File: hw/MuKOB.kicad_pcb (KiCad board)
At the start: 2 copper layers, 123.2 x 125.7 mm, 121 parts, among them J1 UART0 IO01, J10 IO_EX, J11 SPKR_L, J12 SPKR_R, J13 UI 20-RBN, J14 AUDIO, J15 SPI-0, J16 SPI-DISP, J17 SW_MATRIX, J18 UIM 20-FCC, J19 UIM 20-RBN, J2 SERIAL-COMM, J3 KEY_SND_IF, J4 GPIO28, J5 I2C-0, J6 MicroSD-Socket w/Det, J7 KEY-PADDLE, J8 UART1 IO89, J9 UI 20-FCC, Q1 2N3904, SW1 RESET, SW2 RE-SO, SW3 UP, SW4 LF, SW5 EN, SW6 RT, SW7 DN, SW8 RE-AO, SW9 RE-BO, U1 MAX3221, U2 PicoW, U3 MCP23S08-E/SO, U4 TLV70033_SOT23-5, U5 TPA2012D2RTJT, U6 NC7WZ16P6X

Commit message: Main w/ UI - DRC close.
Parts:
- added CF1: 0.1uF, Capacitor_THT:C_Axial_L3.8mm_D2.6mm_P7.50mm_Horizontal, F.Cu at (80.7, 80.3)
- added CF2: 0.1uF, Capacitor_THT:C_Axial_L3.8mm_D2.6mm_P7.50mm_Horizontal, F.Cu at (161.8, 110.3)
- added CF3: 0.1uF, Capacitor_THT:C_Axial_L3.8mm_D2.6mm_P7.50mm_Horizontal, F.Cu at (116.5, 107.3)
- added CF4: 0.1uF, Capacitor_THT:C_Axial_L3.8mm_D2.6mm_P7.50mm_Horizontal, F.Cu at (100.8, 144.0)
- added CF5: 0.1uF, Capacitor_THT:C_Axial_L3.8mm_D2.6mm_P7.50mm_Horizontal, F.Cu at (136.6, 166.7)
- added CFA1: 0.1uF, Capacitor_THT:C_Axial_L3.8mm_D2.6mm_P7.50mm_Horizontal, F.Cu at (68.3, 59.1)
- added CFA2: 0.1uF, Capacitor_THT:C_Axial_L3.8mm_D2.6mm_P7.50mm_Horizontal, F.Cu at (69.7, 117.3)
- added CFA3: 0.1uF, Capacitor_THT:C_Axial_L3.8mm_D2.6mm_P7.50mm_Horizontal, F.Cu at (126.8, 72.2)
- added CFA4: 0.1uF, Capacitor_THT:C_Axial_L3.8mm_D2.6mm_P7.50mm_Horizontal, F.Cu at (95.2, 166.5)
- added CFA5: 0.1uF, Capacitor_THT:C_Axial_L3.8mm_D2.6mm_P7.50mm_Horizontal, F.Cu at (136.6, 145.7)
- added JP-PWR-1: PWR-APWR-Bridge, Connector_PinHeader_2.54mm:PinHeader_2x02_P2.54mm_Vertical, F.Cu at (81.0, 88.4)
- added JP-PWR-2: PWR-APWR-Bridge, Connector_PinHeader_2.54mm:PinHeader_2x02_P2.54mm_Vertical, F.Cu at (84.9, 163.5)
- M_KSI1, M_KSI2, M_KSI3, M_KSI4: footprint MountingHole:MountingHole_3.2mm_M3_ISO7380 -> MountingHole:MountingHole_3.2mm_M3_ISO7380_Pad_TopBottom
- OP8: value IO28-TR -> IO28-ToneR
- moved TP4 53.2 mm to (62.9, 123.7), turned to 90 degrees
- moved TP5 47.9 mm to (66.7, 123.7), turned to 90 degrees
- moved OP1 17.3 mm to (73.7, 98.1), turned to 90 degrees
- moved TP3 15.9 mm to (68.4, 69.5)
- moved TP2 10.4 mm to (156.7, 105.2)
- moved R6 7.73 mm to (61.2, 117.9), turned to 90 degrees
- moved R7 6.41 mm to (53.3, 118.4), turned to 90 degrees
- moved J5 6.26 mm to (93.3, 73.3)
- moved TP1 4.47 mm to (156.7, 112.2)
- moved R1 3.38 mm to (148.5, 155.1)
- moved JP2 3.21 mm to (156.1, 67.5), turned to 180 degrees
- moved C9 2.73 mm to (59.2, 117.2), turned to -90 degrees
- moved R2 2.49 mm to (134.5, 92.4)
- moved U4 2.03 mm to (73.4, 88.6)
- moved C11 2.03 mm to (73.9, 91.4)
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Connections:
- net Net-(J8-Pin_2) renamed /U1_RX
- net Net-(J8-Pin_3) renamed /U1_TX
- net Net-(OP2-A) renamed /U1TX_EXCS
- net Net-(OP2-C) renamed /GPIO08
- net Net-(OP3-A) renamed /U1RX_EXINT
- net Net-(OP3-C) renamed /GPIO09
- C22 pad 2: GND -> GNDA
- C23 pad 2: GND -> GNDA
- C24 pad 2: GND -> GNDA
- C25 pad 2: GND -> GNDA
- C26 pad 2: GND -> GNDA
- C27 pad 2: GND -> GNDA
- J13 pad 11: +3.3V -> +3.3VA
- J13 pad 4: GND -> GNDA
- J17 pad 5: GND -> GNDA
- J18 pad 18: GND -> GNDA
- J18 pad 20: +3.3V -> +3.3VA
- J19 pad 11: +3.3V -> +3.3VA
- J19 pad 4: GND -> GNDA
- J9 pad 18: GND -> GNDA
- J9 pad 20: +3.3V -> +3.3VA
- JP2 pad 1: /KEY- -> /KEY_PDL_DOT-
- JP2 pad 2: /KEY_PDL_DOT- -> /KEY-
- R19 pad 1: GND -> GNDA
- R20 pad 1: GND -> GNDA
- R21 pad 1: GND -> GNDA
- R22 pad 1: GND -> GNDA
- R23 pad 1: GND -> GNDA
- R3 pad 1: +3.3V -> +3.3VA
- RE1 pad S1: GND -> GNDA
- SW2 pad 2: GND -> GNDA
- SW8 pad 2: GND -> Net-(SW8-Pad2)
- SW9 pad 2: GND -> Net-(SW8-Pad2)
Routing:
- net /SW_MTRX: track 0.00 -> 398.6 mm, vias 0 -> 7
- net GND: track 0.00 -> 291.7 mm, vias 0 -> 11
- net /RE_B: track 0.00 -> 255.4 mm, vias 0 -> 3
- net /RE_A: track 0.00 -> 254.1 mm, vias 0 -> 2
- net /DISP_RST-: track 0.00 -> 157.9 mm, vias 0 -> 2
- net /KEY-: track 0.00 -> 156.1 mm
- net +3.3V: track 0.00 -> 145.1 mm, vias 0 -> 10
- net /TONE_GEN_R_SPKR: track 0.00 -> 139.1 mm, vias 0 -> 1
- net /VOLB: track 0.00 -> 139.0 mm, vias 0 -> 1
- net /DISP_BL_LED: track 0.00 -> 138.5 mm, vias 0 -> 4
- net VSYS: track 0.00 -> 133.3 mm, vias 0 -> 2
- net GNDA: track 0.00 -> 126.9 mm, vias 0 -> 11
- net /TCH_IRQ-: track 0.00 -> 126.4 mm, vias 0 -> 2
- net /DISP_D/C-: track 0.00 -> 125.2 mm
- net /VOLA: track 0.00 -> 123.1 mm, vias 0 -> 1
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- added copper zone on F.Cu, net +3.3V
- added copper zone on In1.Cu, net +3.3VA
- added copper zone on B.Cu, net GND
- added copper zone on In2.Cu, net GNDA
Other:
- outline, holes or cut-outs redrawn
- copper layers 2 -> 4

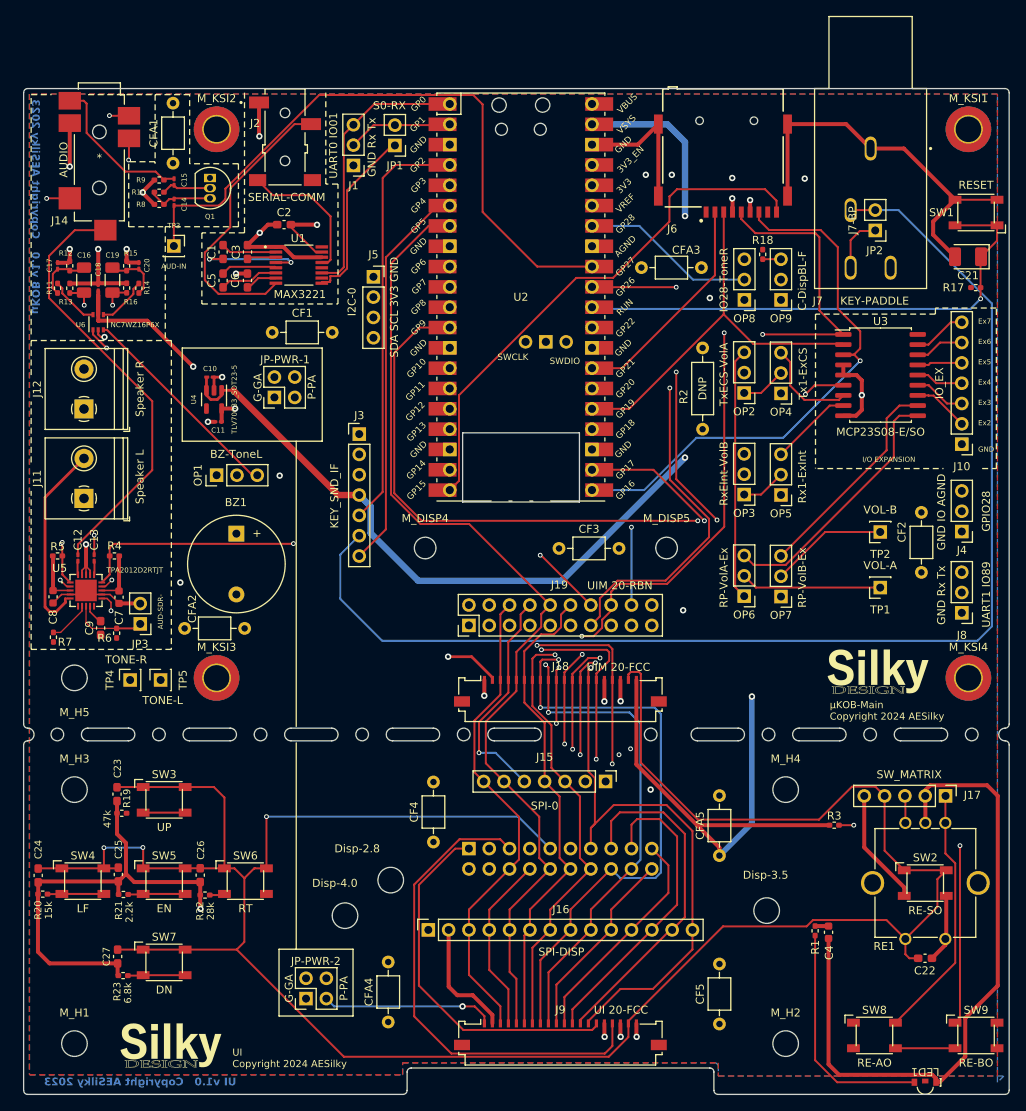
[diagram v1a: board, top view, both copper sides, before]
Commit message: Main PCB v1.0 complete.
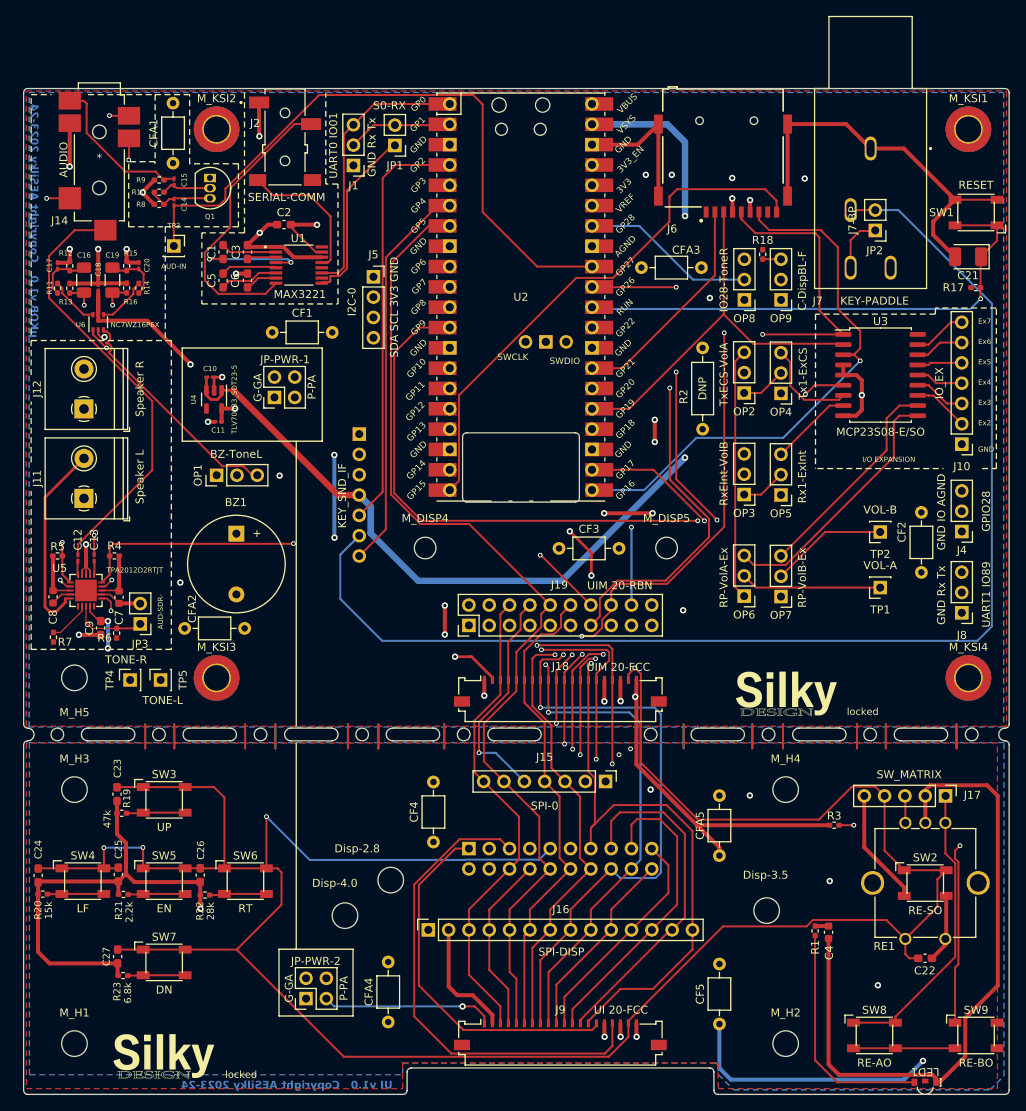
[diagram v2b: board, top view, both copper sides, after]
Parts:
- J3: moved to B.Cu
- moved G1 11.8 mm to (145.0, 125.5)
- moved G2 1.62 mm to (67.2, 170.8)
- turned J3 to 180 degrees
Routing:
- net +3.3V: track 145.1 -> 362.2 mm, vias 10 -> 16
- net GNDA: track 126.9 -> 186.8 mm, vias 11 -> 14
- net GND: track 291.7 -> 329.3 mm
- net +3.3VA: track 103.9 -> 109.7 mm, vias 5 -> 13
- net Net-(SW8-Pad2): track 7.45 -> 12.7 mm
- net Net-(R22-Pad2): track 1.69 -> 6.94 mm
- net /RE_A: track 254.1 -> 259.3 mm
- net /SW_MTRX: track 398.6 -> 402.4 mm, vias 7 -> 8
- net /TONE_GEN_L_SPKR: track 26.1 -> 28.6 mm
- net Net-(R19-Pad2): track 5.25 -> 7.36 mm
- net /TONE_GEN_L: track 100.7 -> 102.1 mm
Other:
- outline, holes or cut-outs redrawn
- board text added: "Copyright AESilky 2023-24"
- board text added: "JP1: Closed for RS232 input Open to use 3.3v (debug) Serial UART0"
- board text added: "OP1:1-2 = BUZZER (No Audio) 2-3 = AUDIO (with Audio, with or w/o Amp)"
- board text added: "OP2,OP3,OP4,OP5:1-2 (no Audio Amp or ExpIO) = UART1 (GP 8&9) on J8 WITH - Audio and Amp OP2,OP3:2-3 OP6,OP7:1-2 = Volume from Pico WITH - Expansion IO OP2,OP3:1-2 OP4,OP5:2-3 OP6,OP7:2-3 = Volume from Expansion IO (with Audio and Amp) ExGP2-7 available on J10"
- board text added: "OP8:1-2 = GP28/ADC2 to J4 & Display Backlight 2-3 = GP28 for Right Tone Gen OP9:1-2 = GP28/ADC2 Drives Display Backlight 2-3 = Fixed Display Backlight"
- board text added: "locked"
- board text removed: "Copyright AESilky 2023"
- board text removed: "UI Copyright 2024 AESilky"
- board text removed: "μKOB-Main Copyright 2024 AESilky"

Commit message: Add 3D components for rendering.
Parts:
- added R24: 10k, Resistor_SMD:R_0402_1005Metric_Pad0.72x0.64mm_HandSolder, F.Cu at (161.0, 166.0)
- added R25: 10k, Resistor_SMD:R_0402_1005Metric_Pad0.72x0.64mm_HandSolder, F.Cu at (163.5, 166.0)
- J15, J3: footprint Connector_PinHeader_2.54mm:PinHeader_1x07_P2.54mm_Vertical -> Connector_PinSocket_2.54mm:PinSocket_1x07_P2.54mm_Vertical
- TP1, TP2, TP3, TP4, TP5: footprint Connector_PinSocket_2.54mm:PinSocket_1x01_P2.54mm_Vertical -> Connector_PinHeader_2.54mm:PinHeader_1x01_P2.54mm_Vertical
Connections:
- SW8 pad 2: Net-(SW8-Pad2) -> GND
- SW9 pad 2: Net-(SW8-Pad2) -> GND
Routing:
- net +3.3V: track 362.2 -> 414.3 mm, vias 16 -> 48
- net GND: track 329.3 -> 345.3 mm
- net Net-(SW8-Pad2): track 12.7 -> 0.00 mm
- net +3.3VA: track 109.7 -> 113.0 mm, vias 13 -> 15
- net /RE_B: track 255.8 -> 258.3 mm
- net /DISP_RST-: track 157.9 -> 160.3 mm
- net /U1_TX: track 35.6 -> 38.0 mm
- net /RE_A: track 259.3 -> 261.7 mm
- net /EX_CS-: track 12.2 -> 9.89 mm
- net /TCH_IRQ-: track 126.5 -> 125.0 mm
- net /P_VOL_A: track 31.4 -> 32.2 mm
- net /SD_TP_EX_MISO: track 71.2 -> 71.7 mm
